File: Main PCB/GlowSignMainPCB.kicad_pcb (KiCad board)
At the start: 2 copper layers, 169.5 x 83.5 mm, 153 parts, among them SW1 TS-1185EC-C-D-B, SW2 TS-1185EC-C-D-B, SW3 TS24CA, U1 S8050, U10 TP4056, U11 DW01A, U12 AO3400A, U13 AP40P05, U14 AP40P05, U15 SS54, U16 AP40P05, U17 SS54, U18 BL1117-33CX, U2 SS54, U20 MSM261D4030H1CPM, U26 M1250RS-02P, U3 SN74LVC2T45DCUR, U4 ESP32-WROOM-32E, U5 FP6276BXR-G1, U6 SS54, U7 CP2102-GMR, U8 UMH3N, U9 FS8205A

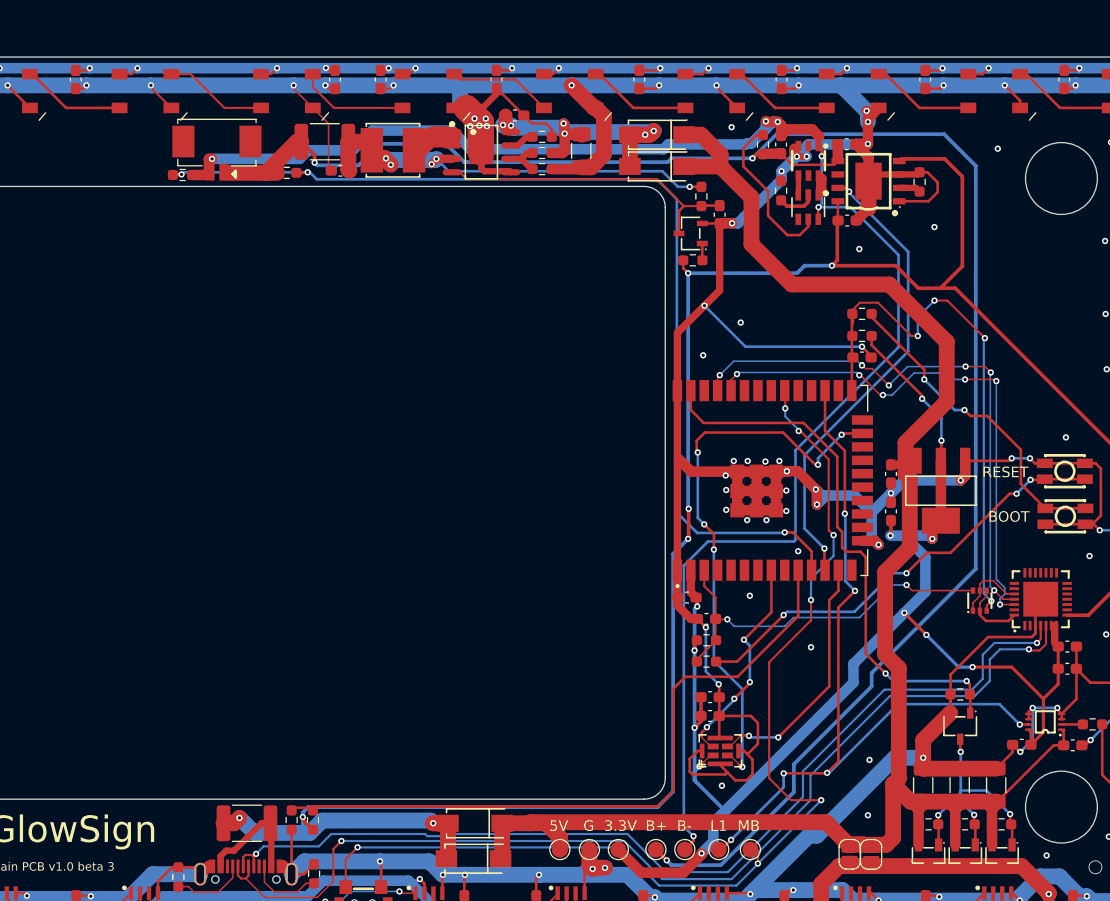
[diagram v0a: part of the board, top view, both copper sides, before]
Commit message: separated battery electronics into separate pcb
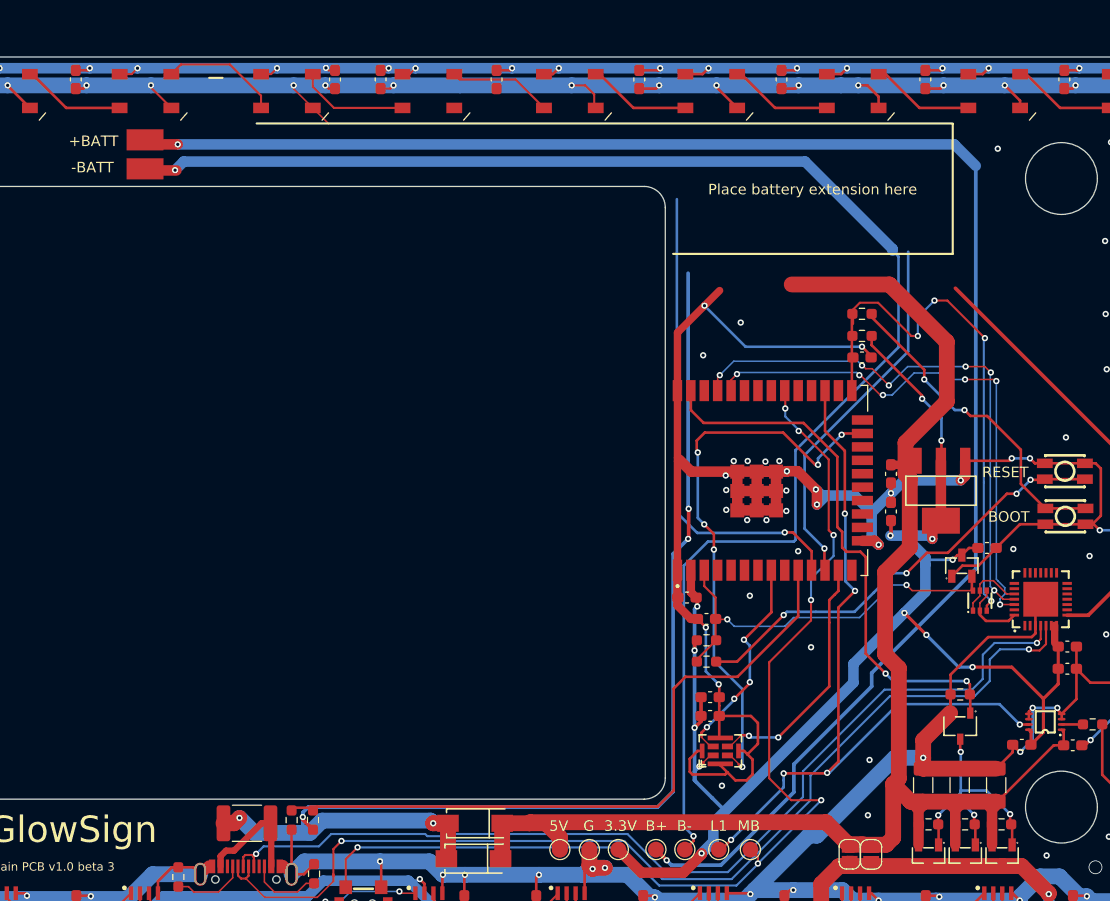
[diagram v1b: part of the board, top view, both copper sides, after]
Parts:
- removed C11, C14: 10uF, Capacitor_SMD:C_0603_1608Metric_Pad1.08x0.95mm_HandSolder
- removed C12, C16: 22uF, Capacitor_SMD:C_0603_1608Metric_Pad1.08x0.95mm_HandSolder
- removed C13: 0.1uf, Capacitor_SMD:C_0603_1608Metric_Pad1.08x0.95mm_HandSolder
- removed C15: 0.1uF, Capacitor_SMD:C_0603_1608Metric_Pad1.08x0.95mm_HandSolder
- removed C17: 100uF, Capacitor_SMD:C_1206_3216Metric_Pad1.33x1.80mm_HandSolder
- removed F2: BSMD1812-300-16V, Fuse:Fuse_1812_4532Metric_Pad1.30x3.40mm_HandSolder
- removed L1: CKCS5040-3_3UH_M, footprint:IND-SMD_L5.0-W5.0
- removed R12, R16, R8, R9: 100K, Resistor_SMD:R_0603_1608Metric_Pad0.98x0.95mm_HandSolder
- removed R13: 1K, Resistor_SMD:R_0603_1608Metric_Pad0.98x0.95mm_HandSolder
- removed R14, R23: 5.1K, Resistor_SMD:R_0603_1608Metric_Pad0.98x0.95mm_HandSolder
- removed R15: 100, Resistor_SMD:R_0603_1608Metric_Pad0.98x0.95mm_HandSolder
- removed R17: 62K, Resistor_SMD:R_0603_1608Metric_Pad0.98x0.95mm_HandSolder
- removed R22: 36K, Resistor_SMD:R_0603_1608Metric_Pad0.98x0.95mm_HandSolder
- removed U1: S8050, footprint:SOT-23-3_L3.0-W1.7-P0.95-LS2.9-BR
- removed U10: TP4056, footprint:ESOP-8_L4.9-W3.9-P1.27-LS6.0-BL-EP
- removed U11: DW01A, footprint:SOT-23-6_L2.9-W1.6-P0.95-LS2.8-BL
- removed U15, U6: SS54, footprint:SMA_L4.4-W2.8-LS5.4-RD
- removed U26: M1250RS-02P, footprint:CONN-SMD_2P-P1.25_L4.4-W7.4
- removed U5: FP6276BXR-G1, footprint:SOP-8_L4.9-W3.9-P1.27-LS6.0-BL-EP
- removed U9: FS8205A, footprint:SOT-23-6_L2.9-W1.6-P0.95-LS2.8-BR
- added C57: 0.1uF, Capacitor_SMD:C_0603_1608Metric_Pad1.08x0.95mm_HandSolder, F.Cu at (217.4, 105.8)
- added P1: Solder_Pad, footprint:Solder pad, F.Cu at (137.6, 67.1)
- added P2: Solder_Pad, footprint:Solder pad, F.Cu at (137.6, 69.8)
- added U19: TPS3839G33DBZR, footprint:SOT-23-3_L2.9-W1.3-P1.90-LS2.4-BR, F.Cu at (215.0, 107.5)
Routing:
- net GND: track 1002.9 -> 915.7 mm, vias 130 -> 117
- net VBUS: track 207.9 -> 155.5 mm, vias 7 -> 5
- net IO26/BATT VOLT: track 95.7 -> 45.8 mm, vias 3 -> 1
- net Net-(C12-Pad1): track 43.2 -> 0.00 mm, vias 5 -> 0
- net Net-(C13-Pad1): track 29.5 -> 0.00 mm
- net Net-(C16-Pad1): track 26.9 -> 0.00 mm, vias 6 -> 0
- net +5V: track 173.9 -> 151.1 mm
- net Net-(R15-Pad1): track 15.3 -> 0.00 mm
- net IO27/BATT CHARGING: track 44.2 -> 35.0 mm, vias 2 -> 1
- net +BATT: track 171.6 -> 162.4 mm, vias 3 -> 2
- net -BATT: track 154.6 -> 145.8 mm, vias 6 -> 2
- net +3V3: track 138.8 -> 144.4 mm, vias 12 -> 13
- net Net-(R22-Pad1): track 3.76 -> 0.00 mm
- net Net-(L1-Pad2): track 3.76 -> 0.00 mm
- net Net-(R13-Pad2): track 3.61 -> 0.00 mm
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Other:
- board text added: "+BATT"
- board text added: "-BATT"
- board text added: "Place battery extension here"

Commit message: updated pcb files
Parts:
- removed the C46 at (131.2, 139.6)
- removed the C47 at (167.9, 139.6)
- removed the D31 at (137.6, 139.3)
- removed the D32 at (164.5, 139.3)
- added JP3: SolderJumper_2_Bridged, Jumper:SolderJumper-2_P1.3mm_Bridged_RoundedPad1.0x1.5mm, F.Cu at (189.0, 120.6)
- added P3: Solder_Pad, footprint:Solder pad, F.Cu at (189.7, 78.1)
- added P4: Solder_Pad, footprint:Solder pad, F.Cu at (199.6, 78.1)
- added P5: Solder_Pad, footprint:Solder pad, F.Cu at (209.6, 78.1)
- added P6: Solder_Pad, footprint:Solder pad, F.Cu at (214.1, 74.6)
- added P7: Solder_Pad, footprint:Solder pad, F.Cu at (214.1, 68.9)
- D26, D27, D28, D29, D30: value WS2812B-4020 -> WS2812B; footprint footprint:LED-SMD_WS2812B-4020 -> LED_SMD:LED_WS2812B_PLCC4_5.0x5.0mm_P3.2mm
- D31: renamed from D33; value WS2812B-4020 -> WS2812B; footprint footprint:LED-SMD_WS2812B-4020 -> LED_SMD:LED_WS2812B_PLCC4_5.0x5.0mm_P3.2mm
- D32: renamed from D34; value WS2812B-4020 -> WS2812B; footprint footprint:LED-SMD_WS2812B-4020 -> LED_SMD:LED_WS2812B_PLCC4_5.0x5.0mm_P3.2mm
- D33: renamed from D35; value WS2812B-4020 -> WS2812B; footprint footprint:LED-SMD_WS2812B-4020 -> LED_SMD:LED_WS2812B_PLCC4_5.0x5.0mm_P3.2mm
- D34: renamed from D36; value WS2812B-4020 -> WS2812B; footprint footprint:LED-SMD_WS2812B-4020 -> LED_SMD:LED_WS2812B_PLCC4_5.0x5.0mm_P3.2mm
- D35: renamed from D37; value WS2812B-4020 -> WS2812B; footprint footprint:LED-SMD_WS2812B-4020 -> LED_SMD:LED_WS2812B_PLCC4_5.0x5.0mm_P3.2mm
- moved C46 1.87 mm to (172.9, 140.0)
- moved C10 0.79 mm to (191.8, 121.2)
- moved C53 0.64 mm to (191.8, 119.7)
- moved D26 0.64 mm to (70.9, 139.0)
- moved D35 0.55 mm to (231.4, 139.0)
- moved C50 0.51 mm to (225.5, 140.1)
- moved C18 0.41 mm to (233.4, 135.5)
- moved TP1 0.36 mm to (192.0, 134.0)
- moved TP2 0.36 mm to (195.0, 134.0)
- moved TP4 0.36 mm to (186.0, 134.0)
- moved TP5 0.36 mm to (188.8, 134.0)
- moved TP6 0.36 mm to (182.5, 134.0)
- moved TP7 0.36 mm to (179.7, 134.0)
- moved TP8 0.36 mm to (176.9, 134.0)
- moved D27 0.30 mm to (83.8, 139.0)
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- renumbered C48 to C46, C49 to C47, C50 to C48, C51 to C49, C52 to C50
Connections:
- C10 pad 2: +3V3 -> Net-(C10-Pad2)
- C53 pad 2: +3V3 -> Net-(C10-Pad2)
- D26 pad 1: Net-(D25-Pad2) -> LED 5V
- D26 pad 2: LED 5V -> Net-(D26-Pad2)
- D26 pad 3: Net-(D26-Pad3) -> GND
- D26 pad 4: GND -> Net-(D25-Pad2)
- D27 pad 1: Net-(D26-Pad3) -> LED 5V
- D27 pad 2: LED 5V -> Net-(D27-Pad2)
- D27 pad 3: Net-(D27-Pad3) -> GND
- D27 pad 4: GND -> Net-(D26-Pad2)
- D28 pad 1: Net-(D27-Pad3) -> LED 5V
- D28 pad 2: LED 5V -> Net-(D28-Pad2)
- D28 pad 3: Net-(D28-Pad3) -> GND
- D28 pad 4: GND -> Net-(D27-Pad2)
- D29 pad 1: Net-(D28-Pad3) -> LED 5V
- D29 pad 2: LED 5V -> Net-(D29-Pad2)
- D29 pad 3: Net-(D29-Pad3) -> GND
- D29 pad 4: GND -> Net-(D28-Pad2)
- D30 pad 1: Net-(D29-Pad3) -> LED 5V
- D30 pad 2: LED 5V -> Net-(D30-Pad2)
- D30 pad 3: Net-(D30-Pad3) -> GND
- D30 pad 4: GND -> Net-(D29-Pad2)
- D31 pad 1: Net-(D32-Pad3) -> LED 5V
- D31 pad 2: LED 5V -> Net-(D31-Pad2)
- D31 pad 3: Net-(D33-Pad3) -> GND
- D31 pad 4: GND -> Net-(D30-Pad2)
- D32 pad 1: Net-(D33-Pad3) -> LED 5V
- D32 pad 2: LED 5V -> Net-(D32-Pad2)
- D32 pad 3: Net-(D34-Pad3) -> GND
- D32 pad 4: GND -> Net-(D31-Pad2)
- D33 pad 1: Net-(D34-Pad3) -> LED 5V
- D33 pad 2: LED 5V -> Net-(D33-Pad2)
- D33 pad 3: Net-(D35-Pad3) -> GND
- D33 pad 4: GND -> Net-(D32-Pad2)
- D34 pad 1: Net-(D35-Pad3) -> LED 5V
- D34 pad 2: LED 5V -> Net-(D34-Pad2)
- D34 pad 3: Net-(D36-Pad3) -> GND
- D34 pad 4: GND -> Net-(D33-Pad2)
- D35 pad 1: Net-(D36-Pad3) -> LED 5V
- D35 pad 2: LED 5V -> (no net)
- D35 pad 3: unconnected-(D37-Pad3) -> GND
- D35 pad 4: GND -> Net-(D34-Pad2)
- U20 pad 1: +3V3 -> Net-(C10-Pad2)
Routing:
- net Net-(D30-Pad2): track 0.00 -> 54.4 mm, vias 0 -> 2
- net Net-(D31-Pad3): track 26.5 -> 0.00 mm, vias 2 -> 0
- net GND: track 915.7 -> 941.1 mm, vias 117 -> 112
- net VBUS: track 155.5 -> 180.6 mm, vias 5 -> 8
- net Net-(D34-Pad3): track 14.9 -> 0.00 mm
- net Net-(D35-Pad3): track 13.5 -> 0.00 mm
- net Net-(D36-Pad3): track 13.4 -> 0.00 mm
- net Net-(D34-Pad2): track 0.00 -> 13.2 mm
- net Net-(D33-Pad3): track 13.1 -> 0.00 mm
- net Net-(D32-Pad3): track 13.1 -> 0.00 mm
- net Net-(D26-Pad3): track 13.0 -> 0.00 mm
- net Net-(D29-Pad3): track 12.9 -> 0.00 mm
- net Net-(D30-Pad3): track 12.9 -> 0.00 mm
- net Net-(D28-Pad3): track 12.9 -> 0.00 mm
- net Net-(D27-Pad3): track 12.9 -> 0.00 mm
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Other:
- outline, holes or cut-outs redrawn
- board text added: "GND"
- board text added: "IO18/ Main Button"
- board text added: "IO26/ BATT VOLT"
- board text added: "IO27/ BATT CHARGING"
- board text added: "LEDs always on"
- board text added: "Microphone on"
- board text added: "VBUS"

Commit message: updated pcb files
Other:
- board text added: "Main PCB v1.0 RC1"
- board text removed: "Main PCB v1.0 beta 3"
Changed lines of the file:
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@@
     (property "Sheetfile" "GlowSignMainPCB.kicad_sch")
     (property "Sheetname" "")
-    (attr exclude_from_pos_files)
+    (attr exclude_from_pos_files exclude_from_bom)
     (fp_text reference "P4" (at 0.1524 -3.1496 unlocked) (layer "F.SilkS") hide
       (effects (font (size 1 1) (thickness 0.15)))
@@
     (property "Sheetfile" "GlowSignMainPCB.kicad_sch")
     (property "Sheetname" "")
-    (attr exclude_from_pos_files)
+    (attr exclude_from_pos_files exclude_from_bom)
     (fp_text reference "P2" (at 0.1524 -3.1496 90 unlocked) (layer "F.SilkS") hide
       (effects (font (size 1 1) (thickness 0.15)))
@@
     (property "Sheetfile" "GlowSignMainPCB.kicad_sch")
     (property "Sheetname" "")
-    (attr exclude_from_pos_files)
+    (attr exclude_from_pos_files exclude_from_bom)
     (fp_text reference "P6" (at 0.1524 -3.1496 90 unlocked) (layer "F.SilkS") hide
       (effects (font (size 1 1) (thickness 0.15)))
@@
     (property "Sheetfile" "GlowSignMainPCB.kicad_sch")
     (property "Sheetname" "")
-    (attr exclude_from_pos_files)
+    (attr exclude_from_pos_files exclude_from_bom)
     (fp_text reference "TP1" (at 0 -1.648) (layer "F.SilkS") hide
       (effects (font (size 1 1) (thickness 0.15)))
@@
     (property "Sheetfile" "GlowSignMainPCB.kicad_sch")
     (property "Sheetname" "")
-    (attr exclude_from_pos_files)
+    (attr exclude_from_pos_files exclude_from_bom)
     (fp_text reference "TP4" (at 0 -1.648) (layer "F.SilkS") hide
       (effects (font (size 1 1) (thickness 0.15)))
@@
     (property "Sheetfile" "GlowSignMainPCB.kicad_sch")
     (property "Sheetname" "")
-    (attr exclude_from_pos_files)
+    (attr exclude_from_pos_files exclude_from_bom)
     (fp_text reference "JP2" (at 0 -1.8 90) (layer "F.SilkS") hide
       (effects (font (size 1 1) (thickness 0.15)))
@@
     (property "Sheetfile" "GlowSignMainPCB.kicad_sch")
     (property "Sheetname" "")
-    (attr exclude_from_pos_files)
+    (attr exclude_from_pos_files exclude_from_bom)
     (fp_text reference "TP7" (at 0 -1.648) (layer "F.SilkS") hide
       (effects (font (size 1 1) (thickness 0.15)))
@@
     (property "Sheetfile" "GlowSignMainPCB.kicad_sch")
     (property "Sheetname" "")
-    (attr exclude_from_pos_files)
+    (attr exclude_from_pos_files exclude_from_bom)
     (fp_text reference "TP8" (at 0 -1.648) (layer "F.SilkS") hide
       (effects (font (size 1 1) (thickness 0.15)))
@@
     (property "Sheetfile" "GlowSignMainPCB.kicad_sch")
     (property "Sheetname" "")
-    (attr exclude_from_pos_files)
+    (attr exclude_from_pos_files exclude_from_bom)
     (fp_text reference "TP2" (at 0 -1.648) (layer "F.SilkS") hide
       (effects (font (size 1 1) (thickness 0.15)))
@@
     (property "Sheetfile" "GlowSignMainPCB.kicad_sch")
     (property "Sheetname" "")
-    (attr exclude_from_pos_files)
+    (attr exclude_from_pos_files exclude_from_bom)
     (fp_text reference "P7" (at 0.1524 -3.1496 90 unlocked) (layer "F.SilkS") hide
       (effects (font (size 1 1) (thickness 0.15)))
@@
     (property "Sheetfile" "GlowSignMainPCB.kicad_sch")
     (property "Sheetname" "")
-    (attr exclude_from_pos_files)
+    (attr exclude_from_pos_files exclude_from_bom)
     (fp_text reference "TP6" (at 0 -1.648) (layer "F.SilkS") hide
       (effects (font (size 1 1) (thickness 0.15)))
@@
     (property "Sheetfile" "GlowSignMainPCB.kicad_sch")
     (property "Sheetname" "")
-    (attr exclude_from_pos_files)
+    (attr exclude_from_pos_files exclude_from_bom)
     (fp_text reference "JP3" (at 3.302 0.0508 90) (layer "F.SilkS") hide
       (effects (font (size 1 1) (thickness 0.15)))
@@
     (property "Sheetfile" "GlowSignMainPCB.kicad_sch")
     (property "Sheetname" "")
-    (attr exclude_from_pos_files)
+    (attr exclude_from_pos_files exclude_from_bom)
     (fp_text reference "P3" (at 0.1524 -3.1496 unlocked) (layer "F.SilkS") hide
       (effects (font (size 1 1) (thickness 0.15)))
@@
     (property "Sheetfile" "GlowSignMainPCB.kicad_sch")
     (property "Sheetname" "")
-    (attr exclude_from_pos_files)
+    (attr exclude_from_pos_files exclude_from_bom)
     (fp_text reference "P1" (at 0.1524 -3.1496 90 unlocked) (layer "F.SilkS") hide
       (effects (font (size 1 1) (thickness 0.15)))
@@
     (property "Sheetfile" "GlowSignMainPCB.kicad_sch")
     (property "Sheetname" "")
-    (attr exclude_from_pos_files)
+    (attr exclude_from_pos_files exclude_from_bom)
     (fp_text reference "JP1" (at 0 -1.8 90) (layer "F.SilkS") hide
       (effects (font (size 1 1) (thickness 0.15)))
@@
     (property "Sheetfile" "GlowSignMainPCB.kicad_sch")
     (property "Sheetname" "")
-    (attr exclude_from_pos_files)
+    (attr exclude_from_pos_files exclude_from_bom)
     (fp_text reference "TP5" (at 0 -1.648) (layer "F.SilkS") hide
       (effects (font (size 1 1) (thickness 0.15)))
@@
     (property "Sheetfile" "GlowSignMainPCB.kicad_sch")
     (property "Sheetname" "")
-    (attr exclude_from_pos_files)
+    (attr exclude_from_pos_files exclude_from_bom)
     (fp_text reference "P5" (at 0.1524 -3.1496 unlocked) (layer "F.SilkS") hide
       (effects (font (size 1 1) (thickness 0.15)))
@@
     (effects (font (size 1 1) (thickness 0.15)))
   )
-  (gr_text "Main PCB v1.0 beta 3" (at 123.0376 135.382) (layer "F.SilkS")
+  (gr_text "Main PCB v1.0 RC1" (at 123.0376 135.382) (layer "F.SilkS")
     (effects (font (size 0.8 0.8) (thickness 0.15)) (justify left))
   )

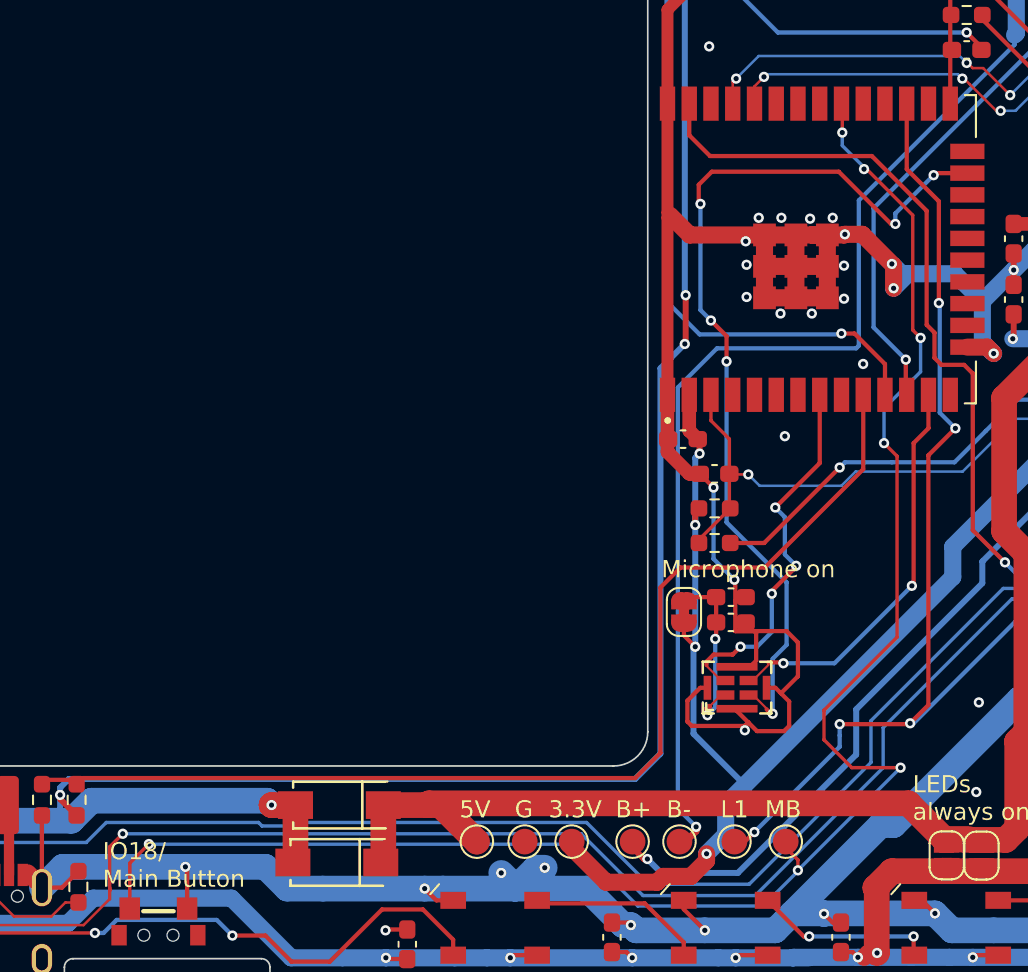
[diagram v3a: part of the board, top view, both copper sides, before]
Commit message: replaced 0603 with 0402 (battery extension)
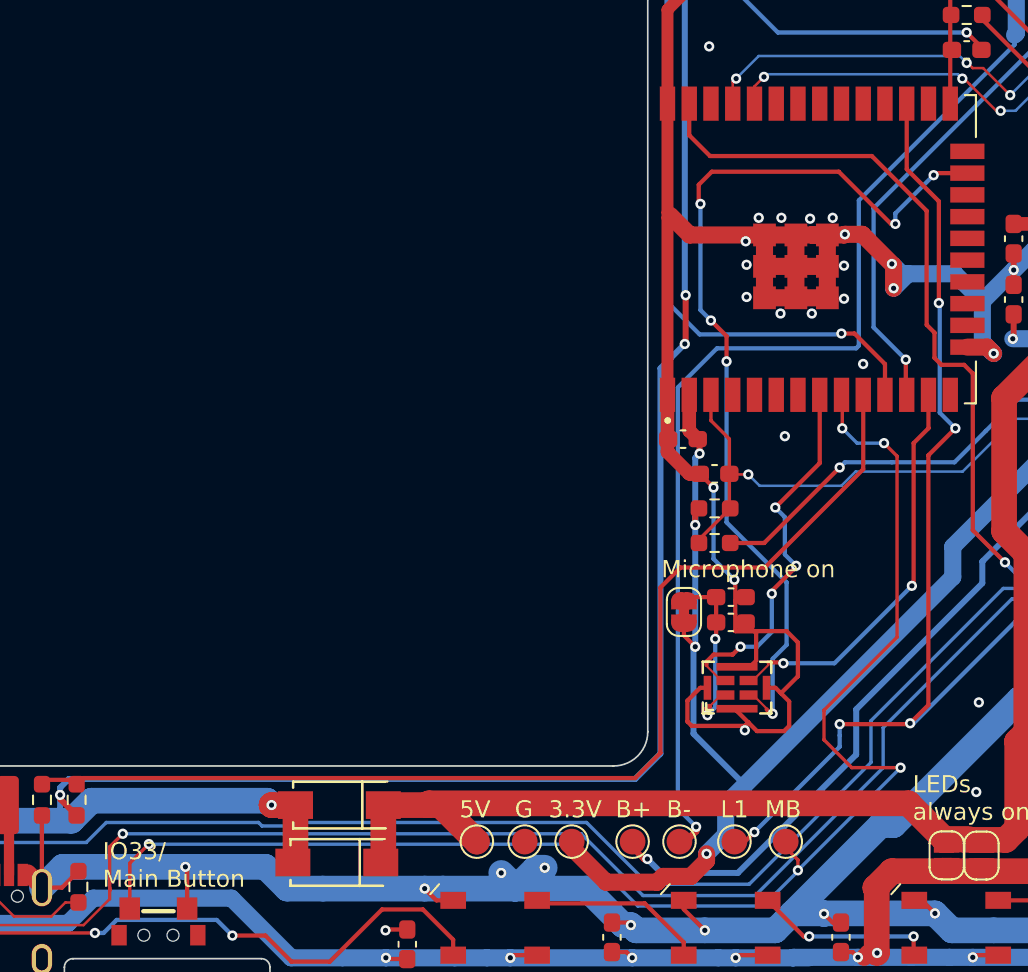
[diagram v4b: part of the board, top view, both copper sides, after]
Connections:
- D35 pad 2: (no net) -> unconnected-(D35-Pad2)
- SW3 pad 4: IO18/MAINBUTTON -> IO33/MAINBUTTON
- U4 pad 30: IO18/MAINBUTTON -> unconnected-(U4-Pad30)
- U4 pad 9: unconnected-(U4-Pad9) -> IO33/MAINBUTTON
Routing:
- net IO18/MAINBUTTON: track 101.9 -> 0.00 mm, vias 7 -> 0
- net IO33/MAINBUTTON: track 0.00 -> 83.9 mm, vias 0 -> 5
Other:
- board text added: "IO33/ Main Button"
- board text removed: "IO18/ Main Button"
